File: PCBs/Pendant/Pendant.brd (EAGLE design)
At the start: 25.4 x 25.4 mm, 17 parts

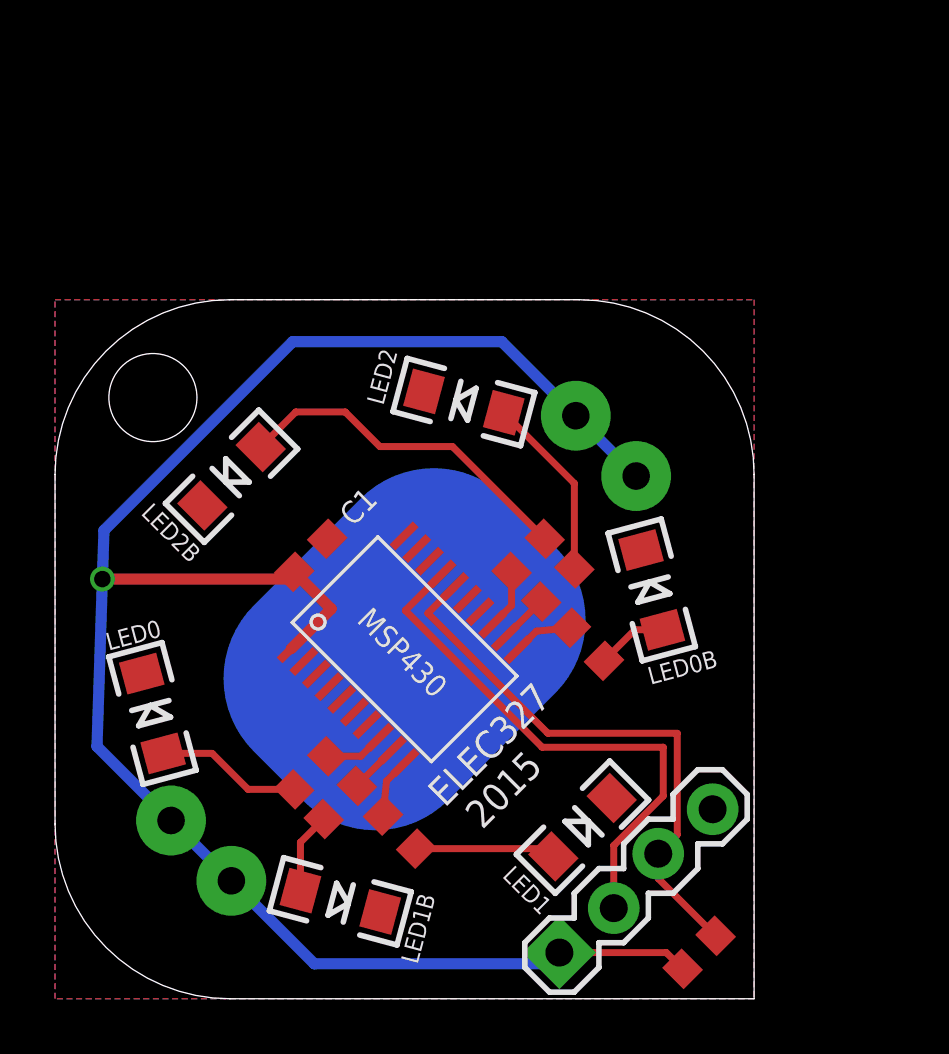
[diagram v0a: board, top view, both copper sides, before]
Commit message: Updated pendant to 2017 version
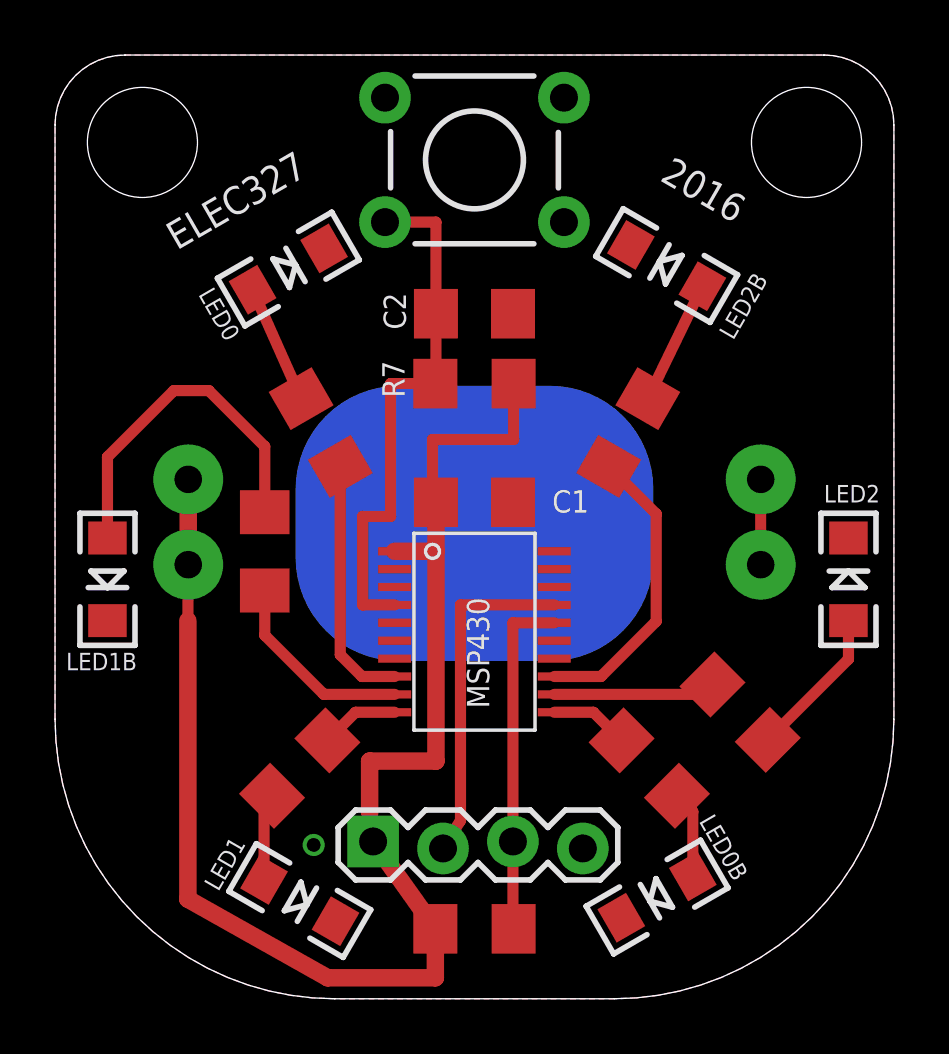
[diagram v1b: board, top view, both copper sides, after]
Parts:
- added C2: 470nF, rcl:C1206
- added R7: (no value), rcl:R1206
- added S1: MOMENTARY-SWITCH-SPST-PTH-6.0MM, SparkFun-Switches:TACTILE_SWITCH_PTH_6.0MM
- C1: device rcl:C0603 -> rcl:C1206
- R1, R2, R3, R4, R5, R6, R_PULLUP_RST: device BiphasicBoard:R0603 -> rcl:R1206
- moved LED2B 17.6 mm to (22.2, 26.6), turned to 150 degrees
- moved LED0 16.9 mm to (8.48, 26.5), turned to 30 degrees
- moved LED2 15.4 mm to (28.8, 15.2), turned to 90 degrees
- moved LED1B 14.4 mm to (1.91, 15.2), turned to 270 degrees
- moved R1 12.4 mm to (9.65, 20.6), turned to 300 degrees
- moved LED0B 11.2 mm to (21.9, 3.70), turned to 210 degrees
- moved LED1 10.6 mm to (8.89, 3.57), turned to 330 degrees
- moved R2 9.53 mm to (7.62, 16.3), turned to 270 degrees
- moved R_PULLUP_RST 8.21 mm to (15.2, 2.54), turned to 180 degrees
- moved R5 8.08 mm to (24.9, 10.4), turned to 315 degrees
- moved JP1 7.94 mm to (11.6, 5.59), turned to 0 degrees
- moved C1 6.25 mm to (15.2, 18.0), turned to 0 degrees
- moved R6 5.76 mm to (20.8, 20.6), turned to 60 degrees
- moved BAT1 5.23 mm to (15.2, 17.3), turned to 0 degrees
- moved R4 5.03 mm to (21.6, 8.38)
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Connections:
- new net N$14: C2.2, MSP430.4, R7.1, S1.3
- net GND: now also C2.1, S1.1
- net VDD: now also R7.2
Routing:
- net N$14: track 0.00 -> 19.6 mm
- net VDD: track 68.0 -> 57.4 mm, vias 1 -> 0
- net N$8: track 2.95 -> 12.9 mm
- net N$5: track 2.20 -> 10.9 mm
- net N$9: track 12.8 -> 4.54 mm
- net _RST: track 20.7 -> 12.6 mm
- net TEST: track 19.9 -> 12.4 mm
- net N$11: track 2.20 -> 9.15 mm
- net N$12: track 1.84 -> 7.24 mm
- net N$1: track 1.85 -> 5.90 mm
- net N$10: track 5.10 -> 3.18 mm
- net N$3: track 6.72 -> 5.55 mm
- net N$7: track 5.30 -> 4.33 mm
- net N$13: track 2.21 -> 2.87 mm
- net N$2: track 2.21 -> 2.87 mm
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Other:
- board size 25.4 x 25.4 mm -> 30.5 x 34.3 mm
- board text added: "2016"
- board text added: "ELEC327"
- board text removed: "ELEC327 2015"

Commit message: Updated Pendant Eagle files
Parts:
- removed LED0, LED0B, LED1B, LED2B: (no value), SparkFun-LED:LED-1206
- removed R_PULLUP_RST: 43k, rcl:R1206
- added LED3, LED4, LED5, LED6, LED7, LED8: (no value), led:CHIPLED_1206
- added R10, R8, R9: (no value), rcl:R1206
- LED1, LED2: device SparkFun-LED:LED-1206 -> led:CHIPLED_1206
- moved LED1 47.6 mm to (25.4, 48.3), turned to 270 degrees
- moved R7 33.4 mm to (46.5, 34.1), turned to 292.5 degrees
- moved LED2 32.8 mm to (9.24, 41.6), turned to 315 degrees
- moved R1 26.9 mm to (16.7, 46.5), turned to 22.5 degrees
- moved R6 26.0 mm to (46.5, 16.7), turned to 247.5 degrees
- moved C1 18.5 mm to (31.8, 26.4), turned to 270 degrees
- moved R2 18.2 mm to (4.28, 34.1), turned to 67.5 degrees
- moved MSP430 16.8 mm to (26.0, 26.2), turned to 180 degrees
- moved S1 15.3 mm to (25.4, 41.9), turned to 90 degrees
- moved C2 14.7 mm to (25.4, 35.6), turned to 0 degrees
- moved BAT1 14.1 mm to (26.2, 26.2)
- moved JP1 12.7 mm to (22.7, 11.7)
- moved R5 11.1 mm to (34.1, 4.28), turned to 202.5 degrees
- moved R3 9.47 mm to (4.28, 16.7), turned to 112.5 degrees
- moved R4 6.42 mm to (16.7, 4.28), turned to 157.5 degrees
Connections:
- net N$1 renamed D5
- net N$2 renamed D4
- net N$5 renamed D6
- removed net N$10: LED1.A, R3.1
- removed net N$11: MSP430.8, R1.2
- removed net N$12: MSP430.9, R2.2
- removed net N$13: MSP430.10, R3.2
- removed net N$9: LED2B.A, R6.2
- new net D1: MSP430.8, R1.1
- new net D2: MSP430.9, R2.1
- new net D3: MSP430.10, R3.1
- new net D7: MSP430.14, R7.1
- new net D8: MSP430.15, R8.1
- new net N$1: LED1.A, R1.2
- new net N$2: LED2.A, R2.2
- new net N$5: LED5.A, R5.2
- net GND: now also LED3.C, LED4.C, LED5.C, LED6.C, LED7.C, LED8.C; no longer LED0.C, LED0B.C, LED1B.C, LED2B.C
- net N$14: now also R9.2; no longer R7.1
- net N$3: now also LED3.A, R3.2; no longer LED2.A, R5.2
- net N$4: now also LED4.A; no longer LED0B.A
- net N$6: now also LED6.A, R6.2; no longer MSP430.7
- net N$7: now also LED7.A, R7.2; no longer LED0.A, R1.1
- net N$8: now also LED8.A, R8.2; no longer LED1B.A, R2.1
- net VDD: now also R10.1, R9.1; no longer R7.2, R_PULLUP_RST.2
- net _RST: now also R10.2; no longer R_PULLUP_RST.1
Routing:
- net D8: track 0.00 -> 72.6 mm
- net D7: track 0.00 -> 66.0 mm
- net D6: track 10.9 -> 49.7 mm
- net D3: track 0.00 -> 30.6 mm
- net D5: track 5.90 -> 36.0 mm
- net D2: track 0.00 -> 22.6 mm
- net VDD: track 57.4 -> 79.8 mm
- net D1: track 0.00 -> 20.9 mm
- net D4: track 2.87 -> 22.9 mm
- net _RST: track 12.6 -> 29.8 mm
- net N$11: track 9.15 -> 0.00 mm
- net N$12: track 7.24 -> 0.00 mm
- net N$8: track 12.9 -> 6.08 mm
- net N$1: track 0.00 -> 6.19 mm
- net N$5: track 0.00 -> 6.14 mm
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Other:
- board size 30.5 x 34.3 mm -> 50.8 x 50.8 mm
- board text added: "2018"
- board text removed: "2016"
